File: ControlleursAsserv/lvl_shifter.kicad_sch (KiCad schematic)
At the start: 3 parts, among them Q1 BSS138

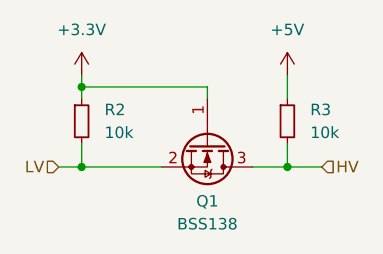
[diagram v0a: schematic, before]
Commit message: Add coders & motors interface
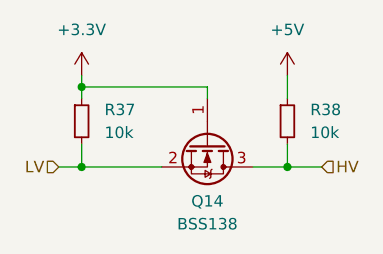
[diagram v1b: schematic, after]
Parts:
- renumbered Q1 to Q14, R2 to R37, R3 to R38
